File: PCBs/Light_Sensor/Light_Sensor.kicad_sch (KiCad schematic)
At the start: 5 parts, among them J2 Conn_01x03

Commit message: latest PCBs
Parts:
- D1: footprint Artisyn_Components:DIODE_0805 -> Diode_THT:D_DO-15_P5.08mm_Vertical_AnodeUp
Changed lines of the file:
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@@
       (effects (font (size 1.27 1.27)) (justify left))
     )
-    (property "Footprint" "Artisyn_Components:DIODE_0805" (at 82.55 83.82 0)
+    (property "Footprint" "Diode_THT:D_DO-15_P5.08mm_Vertical_AnodeUp" (at 82.55 83.82 0)
       (effects (font (size 1.27 1.27)) hide)
     )

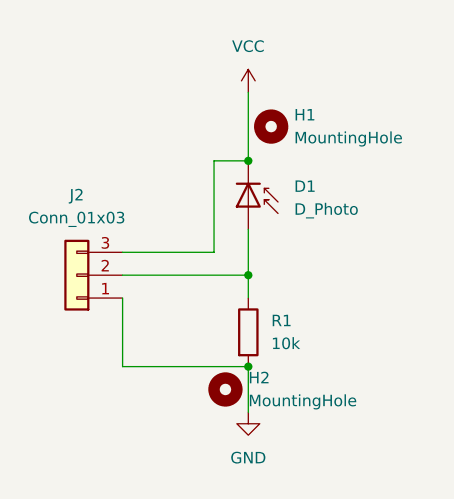
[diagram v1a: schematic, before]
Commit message: fixed PCB layout and updated gbr and drl files
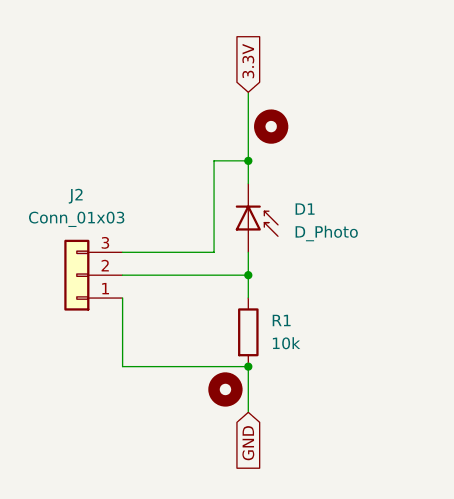
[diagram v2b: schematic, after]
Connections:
- net VCC renamed 3.3V
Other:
- moved on the sheet: D1
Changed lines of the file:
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@@
   (junction (at 82.55 102.87) (diameter 0) (color 0 0 0 0)
   )
-  (wire (pts (xy 82.55 87.63) (xy 82.55 92.71))
+  (wire (pts (xy 82.55 90.17) (xy 82.55 92.71))
     (stroke (width 0) (type default))
   )
   (wire (pts (xy 68.58 92.71) (xy 82.55 92.71))
+    (stroke (width 0) (type default))
+  )
+  (wire (pts (xy 82.55 82.55) (xy 82.55 80.01))
     (stroke (width 0) (type default))
   )
@@
     (stroke (width 0) (type default))
   )
-  (symbol (lib_id "power:GND") (at 82.55 107.95 0) (unit 1)
-    (in_bom yes) (on_board yes) (dnp no) (fields_autoplaced)
-    (property "Reference" "#PWR02" (at 82.55 114.3 0)
-      (effects (font (size 1.27 1.27)) hide)
+  (global_label "GND" (shape input) (at 82.55 107.95 270) (fields_autoplaced)
+    (effects (font (size 1.27 1.27)) (justify right))
+    (property "Intersheetrefs" "${INTERSHEET_REFS}" (at 82.55 114.8057 90)
+      (effects (font (size 1.27 1.27)) (justify right) hide)
     )
-    (property "Value" "GND" (at 82.55 113.03 0)
-      (effects (font (size 1.27 1.27)))
-    )
-    (property "Footprint" "" (at 82.55 107.95 0)
-      (effects (font (size 1.27 1.27)) hide)
-    )
-    (property "Datasheet" "" (at 82.55 107.95 0)
-      (effects (font (size 1.27 1.27)) hide)
-    )
-    (pin "1")
-    (instances
-      (project "Light_Sensor"
-        (path "/cf896358-3be7-4371-9c30-a1da9e460129"
-          (reference "#PWR02") (unit 1)
-        )
-      )
+  )
+  (global_label "3.3V" (shape input) (at 82.55 72.39 90) (fields_autoplaced)
+    (effects (font (size 1.27 1.27)) (justify left))
+    (property "Intersheetrefs" "${INTERSHEET_REFS}" (at 82.55 65.2924 90)
+      (effects (font (size 1.27 1.27)) (justify left) hide)
     )
   )
@@
     (in_bom yes) (on_board yes) (dnp no) (fields_autoplaced)
     (property "Reference" "H2" (at 82.55 104.14 0)
-      (effects (font (size 1.27 1.27)) (justify left))
+      (effects (font (size 1.27 1.27)) (justify left) hide)
     )
     (property "Value" "MountingHole" (at 82.55 106.68 0)
-      (effects (font (size 1.27 1.27)) (justify left))
+      (effects (font (size 1.27 1.27)) (justify left) hide)
     )
     (property "Footprint" "MountingHole:MountingHole_2.7mm" (at 80.01 105.41 0)
@@
     )
   )
-  (symbol (lib_id "Device:D_Photo") (at 82.55 85.09 270) (unit 1)
+  (symbol (lib_id "Device:D_Photo") (at 82.55 87.63 270) (unit 1)
     (in_bom yes) (on_board yes) (dnp no) (fields_autoplaced)
-    (property "Reference" "D1" (at 87.63 82.8675 90)
+    (property "Reference" "D1" (at 87.63 85.4075 90)
       (effects (font (size 1.27 1.27)) (justify left))
     )
-    (property "Value" "D_Photo" (at 87.63 85.4075 90)
+    (property "Value" "D_Photo" (at 87.63 87.9475 90)
       (effects (font (size 1.27 1.27)) (justify left))
     )
-    (property "Footprint" "Diode_THT:D_DO-15_P5.08mm_Vertical_AnodeUp" (at 82.55 83.82 0)
+    (property "Footprint" "Diode_THT:D_DO-15_P5.08mm_Vertical_AnodeUp" (at 82.55 86.36 0)
       (effects (font (size 1.27 1.27)) hide)
     )
-    (property "Datasheet" "~" (at 82.55 83.82 0)
+    (property "Datasheet" "~" (at 82.55 86.36 0)
       (effects (font (size 1.27 1.27)) hide)
     )
@@
     (in_bom yes) (on_board yes) (dnp no) (fields_autoplaced)
     (property "Reference" "H1" (at 87.63 74.93 0)
-      (effects (font (size 1.27 1.27)) (justify left))
+      (effects (font (size 1.27 1.27)) (justify left) hide)
     )
     (property "Value" "MountingHole" (at 87.63 77.47 0)
-      (effects (font (size 1.27 1.27)) (justify left))
+      (effects (font (size 1.27 1.27)) (justify left) hide)
     )
     (property "Footprint" "MountingHole:MountingHole_2.7mm" (at 85.09 76.2 0)
@@
         )
       )
-    )
-  )
-  (symbol (lib_id "power:VCC") (at 82.55 72.39 0) (unit 1)
-    (in_bom yes) (on_board yes) (dnp no) (fields_autoplaced)
-    (property "Reference" "#PWR01" (at 82.55 76.2 0)
-      (effects (font (size 1.27 1.27)) hide)
-    )
-    (property "Value" "VCC" (at 82.55 67.31 0)
-      (effects (font (size 1.27 1.27)))
-    )
-    (property "Footprint" "" (at 82.55 72.39 0)
-      (effects (font (size 1.27 1.27)) hide)
-    )
-    (property "Datasheet" "" (at 82.55 72.39 0)
-      (effects (font (size 1.27 1.27)) hide)
-    )
-    (pin "1")
-    (instances
-      (project "Light_Sensor"
-        (path "/cf896358-3be7-4371-9c30-a1da9e460129"
-          (reference "#PWR01") (unit 1)
-        )
-      )

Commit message: fixed trace
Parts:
- D1: footprint Diode_THT:D_DO-15_P5.08mm_Vertical_AnodeUp -> Connector_Wire:SolderWire-0.1sqmm_1x02_P3.6mm_D0.4mm_OD1mm
- J2: footprint Connector_JST:JST_EH_B3B-EH-A_1x03_P2.50mm_Vertical -> Connector_PinSocket_2.54mm:PinSocket_1x03_P2.54mm_Vertical
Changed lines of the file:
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@@
       (effects (font (size 1.27 1.27)) (justify left))
     )
-    (property "Footprint" "Diode_THT:D_DO-15_P5.08mm_Vertical_AnodeUp" (at 82.55 86.36 0)
+    (property "Footprint" "Connector_Wire:SolderWire-0.1sqmm_1x02_P3.6mm_D0.4mm_OD1mm" (at 82.55 86.36 0)
       (effects (font (size 1.27 1.27)) hide)
     )
@@
       (effects (font (size 1.27 1.27)))
     )
-    (property "Footprint" "Connector_JST:JST_EH_B3B-EH-A_1x03_P2.50mm_Vertical" (at 63.5 92.71 0)
+    (property "Footprint" "Connector_PinSocket_2.54mm:PinSocket_1x03_P2.54mm_Vertical" (at 63.5 92.71 0)
       (effects (font (size 1.27 1.27)) hide)
     )
